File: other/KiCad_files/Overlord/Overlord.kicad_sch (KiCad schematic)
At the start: 136 parts, among them J1 39502-1011, J10 USB_B_Micro, J2 39502-1011, J3 39502-1011, J4 Conn_01x12_Pin, J5 Conn_01x10_Pin, J6 Conn_01x11_Pin, J7 Conn_01x11_Pin

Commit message: minor PCB update
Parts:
- removed C8: 10uF, Capacitor_SMD:C_0805_2012Metric_Pad1.18x1.45mm_HandSolder, symbol Device:C
- added C4: 22uF, Capacitor_SMD:C_0805_2012Metric_Pad1.18x1.45mm_HandSolder, symbol Device:C
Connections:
- net ESP_EN: now also C4.1
- net GND: now also C4.2
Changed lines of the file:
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@@
 	)
 	(junction
+		(at 58.42 142.24)
+		(diameter 0)
+		(color 0 0 0 0)
+	)
+	(junction
 		(at 187.96 39.37)
 		(diameter 0)
@@
 	)
 	(junction
-		(at 58.42 142.24)
-		(diameter 0)
-		(color 0 0 0 0)
-	)
-	(junction
 		(at 85.09 187.96)
 		(diameter 0)
@@
 	)
 	(symbol
-		(lib_id "Device:C")
-		(at 58.42 138.43 0)
-		(unit 1)
-		(exclude_from_sim no)
-		(in_bom yes)
-		(on_board yes)
-		(dnp no)
-		(property "Reference" "C8"
-			(at 59.944 137.16 90)
-			(effects
-				(font
-					(size 1.27 1.27)
-				)
-				(justify left)
-			)
-		)
-		(property "Value" "10uF"
-			(at 61.976 140.97 90)
-			(effects
-				(font
-					(size 1.27 1.27)
-				)
-				(justify left)
-			)
-		)
-		(property "Footprint" "Capacitor_SMD:C_0805_2012Metric_Pad1.18x1.45mm_HandSolder"
-			(at 59.3852 142.24 0)
-			(effects
-				(font
-					(size 1.27 1.27)
-				)
-				(hide yes)
-			)
-		)
-		(property "Datasheet" "https://www.mouser.se/ProductDetail/Samsung-Electro-Mechanics/CL21A106KOQNNNE?qs=349EhDEZ59qKIX0T0PKtPw%3D%3D"
-			(at 58.42 138.43 0)
-			(effects
-				(font
-					(size 1.27 1.27)
-				)
-				(hide yes)
-			)
-		)
-		(property "Description" "Unpolarized capacitor"
-			(at 58.42 138.43 0)
-			(effects
-				(font
-					(size 1.27 1.27)
-				)
-				(hide yes)
-			)
-		)
-		(pin "1"
-		)
-		(pin "2"
-		)
-		(instances
-			(project "Overlord"
-				(path "/b05fe6d7-2198-4616-b68d-60ce1e3d6296"
-					(reference "C8")
-					(unit 1)
-				)
-			)
-		)
-	)
-	(symbol
 		(lib_id "power:+3.3V")
 		(at 240.03 172.72 0)
@@
 					(unit 1)
 				)
+			)
+		)
+	)
+	(symbol
+		(lib_id "Device:C")
+		(at 58.42 138.43 0)
+		(unit 1)
+		(exclude_from_sim no)
+		(in_bom yes)
+		(on_board yes)
+		(dnp no)
+		(property "Reference" "C4"
+			(at 63.754 138.43 0)
+			(effects
+				(font
+					(size 1.27 1.27)
+				)
+				(justify right)
+			)
+		)
+		(property "Value" "22uF"
+			(at 64.262 140.716 0)
+			(effects
+				(font
+					(size 1.27 1.27)
+				)
+				(justify right)
+			)
+		)
+		(property "Footprint" "Capacitor_SMD:C_0805_2012Metric_Pad1.18x1.45mm_HandSolder"
+			(at 59.3852 142.24 0)
+			(effects
+				(font
+					(size 1.27 1.27)
+				)
+				(hide yes)
+			)
+		)
+		(property "Datasheet" "https://www.mouser.se/ProductDetail/Samsung-Electro-Mechanics/CL21A226MAYNNNE?qs=sGAEpiMZZMsh%252B1woXyUXj9e2R%2FOkAO5o4FNiyGuFzx8%3D"
+			(at 58.42 138.43 0)
+			(effects
+				(font
+					(size 1.27 1.27)
+				)
+				(hide yes)
+			)
+		)
+		(property "Description" "Unpolarized capacitor"
+			(at 58.42 138.43 0)
+			(effects
+				(font
+					(size 1.27 1.27)
+				)
+				(hide yes)
+			)
+		)
+		(pin "2"
+		)
+		(pin "1"
+		)
+		(instances
+			(project "Overlord"
+				(path "/b05fe6d7-2198-4616-b68d-60ce1e3d6296"
+					(reference "C4")
+					(unit 1)
+				)

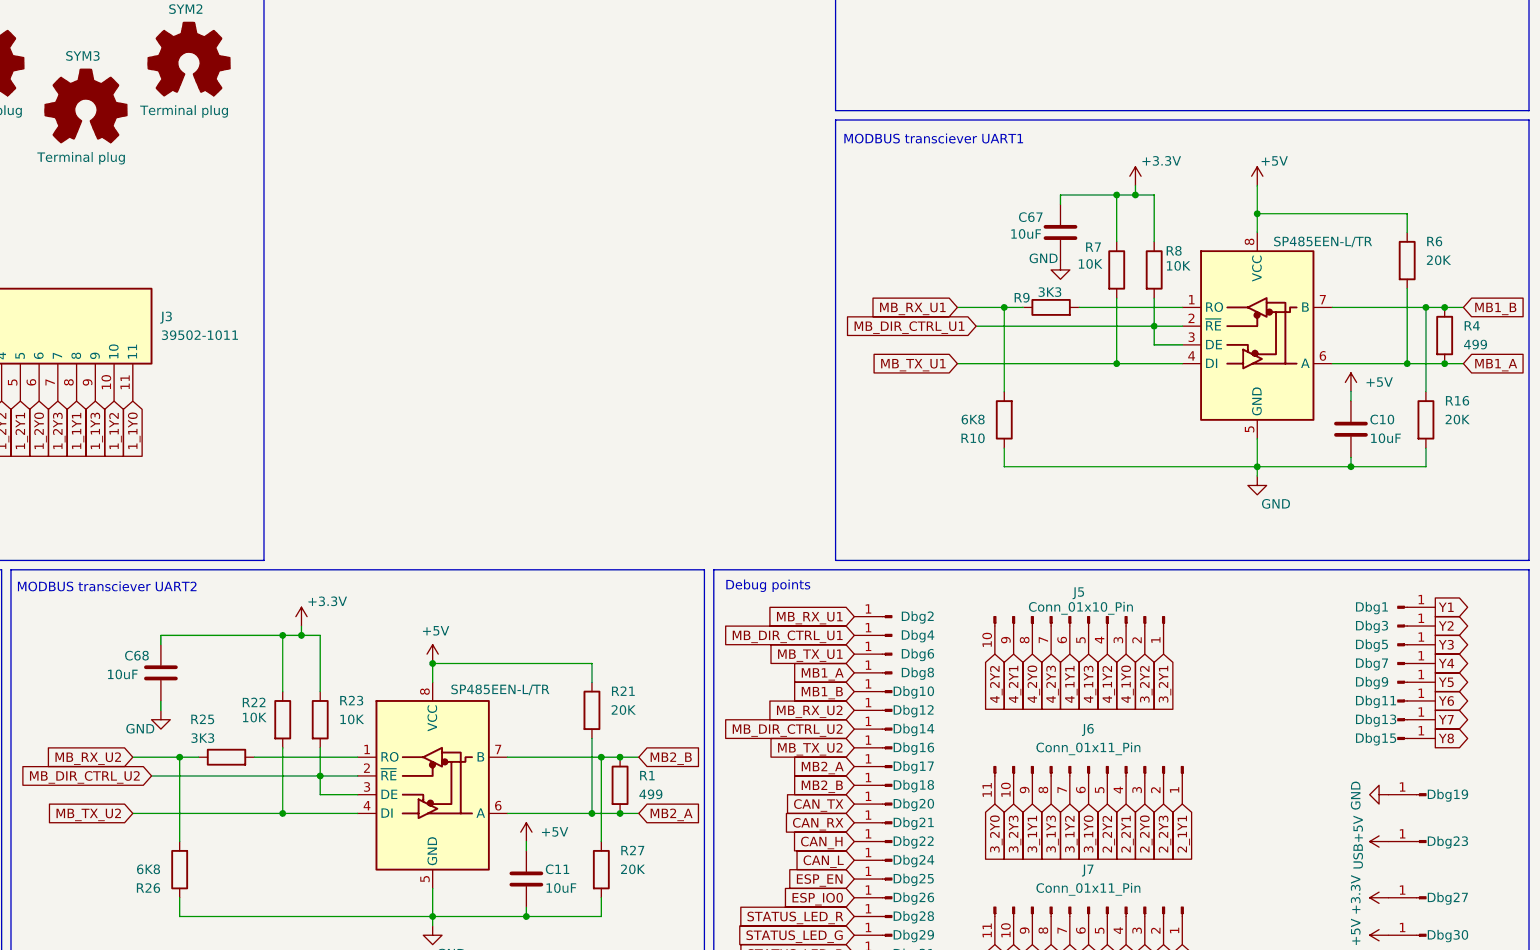
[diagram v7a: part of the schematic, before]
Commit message: returned 10k pullup on RO for Modbus as testing showed insufficient pull without
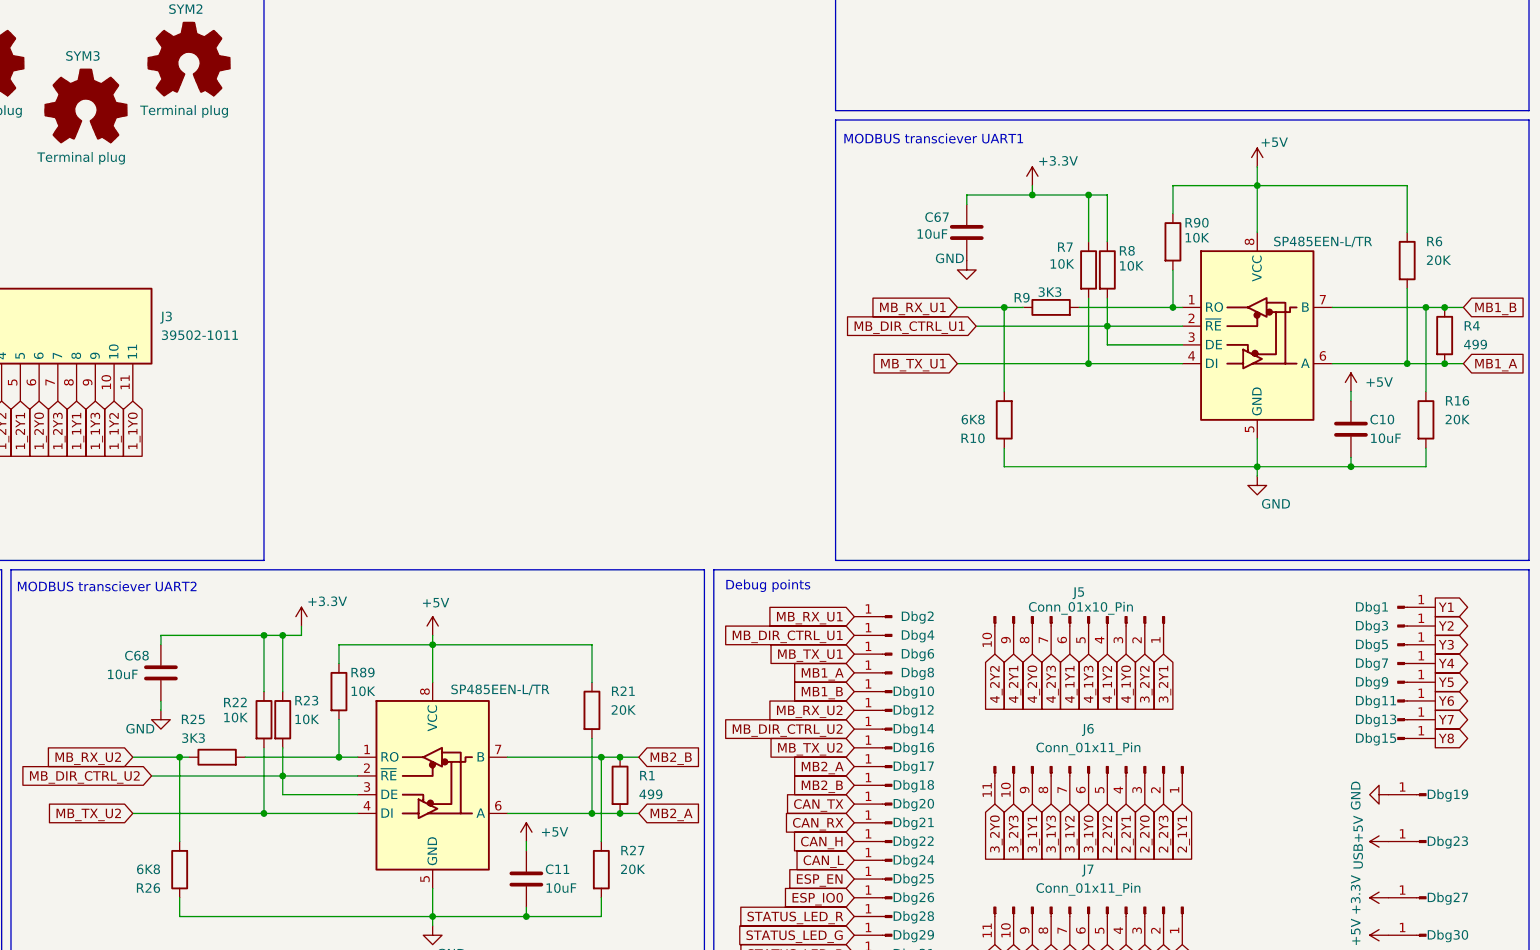
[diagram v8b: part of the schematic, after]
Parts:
- added R89, R90: 10K, Resistor_SMD:R_0805_2012Metric_Pad1.20x1.40mm_HandSolder, symbol Device:R
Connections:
- net +5V: now also R89.1, R90.1
- net at R9.2, SP485EEN-L/TR_1.1 (RO): now also R90.2
- net at R25.2, SP485EEN-L/TR_2.1 (RO): now also R89.2
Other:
- moved on the sheet: C67, R22, R23, R25, R7, R8
